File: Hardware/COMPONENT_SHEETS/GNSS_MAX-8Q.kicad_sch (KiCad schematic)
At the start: 12 parts, among them J2 Conn_Coaxial, Q1 SI1040X-T1-GE3, U4 MAX-8Q

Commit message: Corrected PCB edge cuts, removed components
Will be mimicking layout done by Seth Sievers
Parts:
- renumbered C4 to C5, C5 to C6, R3 to R1, R4 to R2, R5 to R3, U4 to U3
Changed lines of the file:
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@@
   (symbol (lib_id "Data_Collection_KiCAD_Project-rescue:GND-power-Data_Collection_KiCAD_Project-rescue") (at 101.6 165.1 0)
     (in_bom yes) (on_board yes)
-    (property "Reference" "#PWR018" (id 0) (at 101.6 171.45 0)
+    (property "Reference" "#PWR023" (id 0) (at 101.6 171.45 0)
       (effects (font (size 1.27 1.27)) hide)
     )
@@
   (symbol (lib_id "Data_Collection_KiCAD_Project-rescue:R-Device-Data_Collection_KiCAD_Project-rescue") (at 119.38 140.97 180)
     (in_bom yes) (on_board yes)
-    (property "Reference" "R5" (id 0) (at 117.602 142.1384 0)
+    (property "Reference" "R3" (id 0) (at 117.602 142.1384 0)
       (effects (font (size 1.27 1.27)) (justify left))
     )
@@
   (symbol (lib_id "Data_Collection_KiCAD_Project-rescue:R-Device-Data_Collection_KiCAD_Project-rescue") (at 110.49 158.75 0)
     (in_bom yes) (on_board yes)
-    (property "Reference" "R4" (id 0) (at 112.268 157.5816 0)
+    (property "Reference" "R2" (id 0) (at 112.268 157.5816 0)
       (effects (font (size 1.27 1.27)) (justify left))
     )
@@
   (symbol (lib_id "Data_Collection_KiCAD_Project-rescue:GND-power-Data_Collection_KiCAD_Project-rescue") (at 124.46 146.05 0)
     (in_bom yes) (on_board yes)
-    (property "Reference" "#PWR019" (id 0) (at 124.46 152.4 0)
+    (property "Reference" "#PWR024" (id 0) (at 124.46 152.4 0)
       (effects (font (size 1.27 1.27)) hide)
     )
@@
   (symbol (lib_id "Data_Collection_KiCAD_Project-rescue:R-Device-Data_Collection_KiCAD_Project-rescue") (at 92.71 140.97 0) (mirror y)
     (in_bom yes) (on_board yes)
-    (property "Reference" "R3" (id 0) (at 90.932 139.8016 0)
+    (property "Reference" "R1" (id 0) (at 90.932 139.8016 0)
       (effects (font (size 1.27 1.27)) (justify left))
     )
@@
   (symbol (lib_id "Data_Collection_KiCAD_Project-rescue:+3.3V-power-Data_Collection_KiCAD_Project-rescue") (at 182.88 60.96 0)
     (in_bom yes) (on_board yes)
-    (property "Reference" "#PWR021" (id 0) (at 182.88 64.77 0)
+    (property "Reference" "#PWR026" (id 0) (at 182.88 64.77 0)
       (effects (font (size 1.27 1.27)) hide)
     )
@@
   (symbol (lib_id "Data_Collection_KiCAD_Project-rescue:GND-power-Data_Collection_KiCAD_Project-rescue") (at 195.58 99.06 0)
     (in_bom yes) (on_board yes)
-    (property "Reference" "#PWR022" (id 0) (at 195.58 105.41 0)
+    (property "Reference" "#PWR027" (id 0) (at 195.58 105.41 0)
       (effects (font (size 1.27 1.27)) hide)
     )
@@
   (symbol (lib_id "Data_Collection_KiCAD_Project-rescue:MAX-8Q-RF_GPS-Data_Collection_KiCAD_Project-rescue") (at 195.58 81.28 0)
     (in_bom yes) (on_board yes)
-    (property "Reference" "U4" (id 0) (at 195.58 53.34 0))
+    (property "Reference" "U3" (id 0) (at 195.58 53.34 0))
     (property "Value" "MAX-8Q" (id 1) (at 195.58 55.88 0))
     (property "Footprint" "RF_GPS:ublox_MAX" (id 2) (at 205.74 97.79 0)
@@
   (symbol (lib_id "Data_Collection_KiCAD_Project-rescue:GND-power-Data_Collection_KiCAD_Project-rescue") (at 30.48 49.53 0)
     (in_bom yes) (on_board yes)
-    (property "Reference" "#PWR017" (id 0) (at 30.48 55.88 0)
+    (property "Reference" "#PWR022" (id 0) (at 30.48 55.88 0)
       (effects (font (size 1.27 1.27)) hide)
     )
@@
   (symbol (lib_id "Data_Collection_KiCAD_Project-rescue:C-Device-Data_Collection_KiCAD_Project-rescue") (at 30.48 43.18 0)
     (in_bom yes) (on_board yes)
-    (property "Reference" "C4" (id 0) (at 33.401 42.0116 0)
+    (property "Reference" "C5" (id 0) (at 33.401 42.0116 0)
       (effects (font (size 1.27 1.27)) (justify left))
     )
@@
   (symbol (lib_id "Data_Collection_KiCAD_Project-rescue:+3.3V-power-Data_Collection_KiCAD_Project-rescue") (at 30.48 36.83 0)
     (in_bom yes) (on_board yes)
-    (property "Reference" "#PWR016" (id 0) (at 30.48 40.64 0)
+    (property "Reference" "#PWR021" (id 0) (at 30.48 40.64 0)
       (effects (font (size 1.27 1.27)) hide)
     )
@@
   (symbol (lib_id "Data_Collection_KiCAD_Project-rescue:C-Device-Data_Collection_KiCAD_Project-rescue") (at 40.64 43.18 0)
     (in_bom yes) (on_board yes)
-    (property "Reference" "C5" (id 0) (at 43.561 42.0116 0)
+    (property "Reference" "C6" (id 0) (at 43.561 42.0116 0)
       (effects (font (size 1.27 1.27)) (justify left))
     )
@@
   (symbol (lib_id "Data_Collection_KiCAD_Project-rescue:GND-power-Data_Collection_KiCAD_Project-rescue") (at 238.76 86.36 0)
     (in_bom yes) (on_board yes)
-    (property "Reference" "#PWR023" (id 0) (at 238.76 92.71 0)
+    (property "Reference" "#PWR028" (id 0) (at 238.76 92.71 0)
       (effects (font (size 1.27 1.27)) hide)
     )
@@
   (symbol (lib_id "Data_Collection_KiCAD_Project-rescue:GND-power-Data_Collection_KiCAD_Project-rescue") (at 166.37 93.98 0)
     (in_bom yes) (on_board yes)
-    (property "Reference" "#PWR020" (id 0) (at 166.37 100.33 0)
-      (effects (font (size 1.27 1.27)) hide)
-    )
+    (property "Reference" "#PWR025" (id 0) (at 166.37 100.33 0)
+      (effects (font (size 1.27 1.27)) hide)
+    )

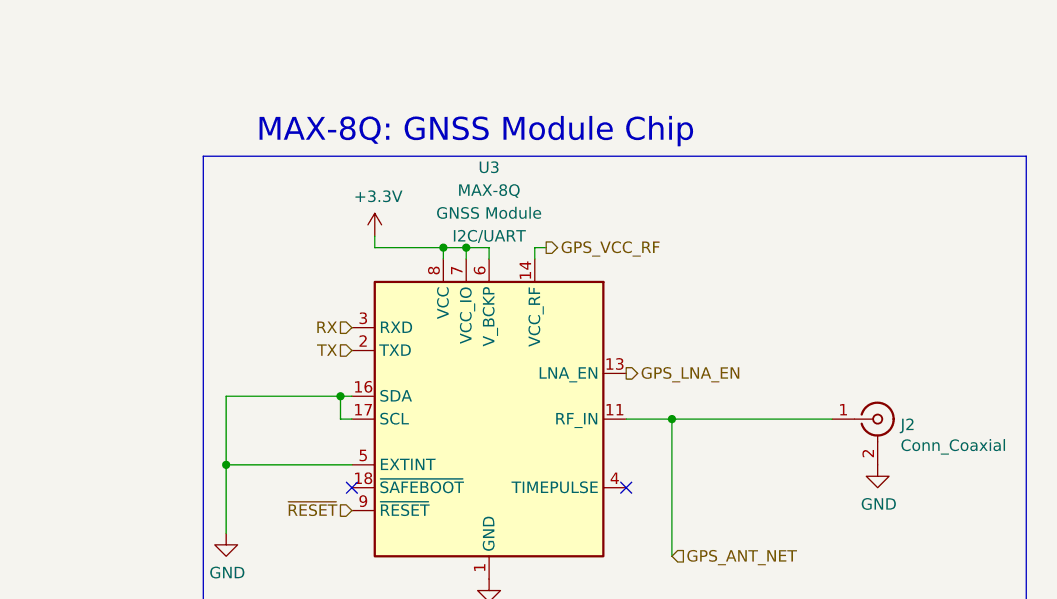
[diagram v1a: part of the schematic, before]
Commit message: Organized components, arranged filter caps
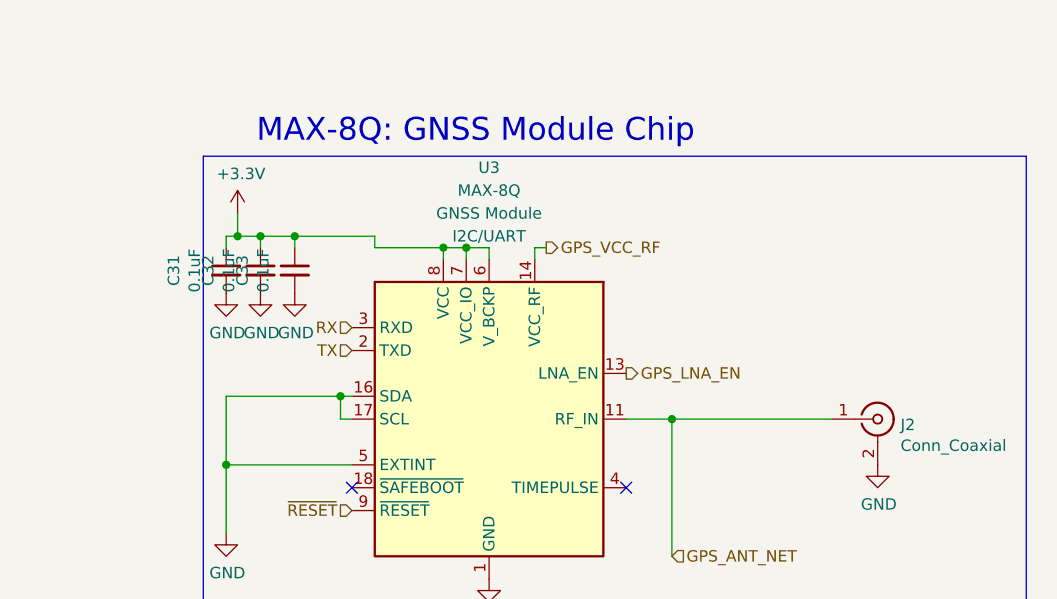
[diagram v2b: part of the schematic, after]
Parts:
- added C31, C32, C33: 0.1uF, Capacitor_SMD:C_0603_1608Metric_Pad1.08x0.95mm_HandSolder, symbol Data_Collection_KiCAD_Project-rescue:C_Small-Device-Data_Collection_KiCAD_Proje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
- Q1: footprint SC-89:SC-89 -> Package_TO_SOT_SMD:TSOT-23-6_HandSoldering
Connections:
- net +3V3: now also C31.1, C32.1, C33.1
- net GND: now also C31.2, C32.2, C33.2

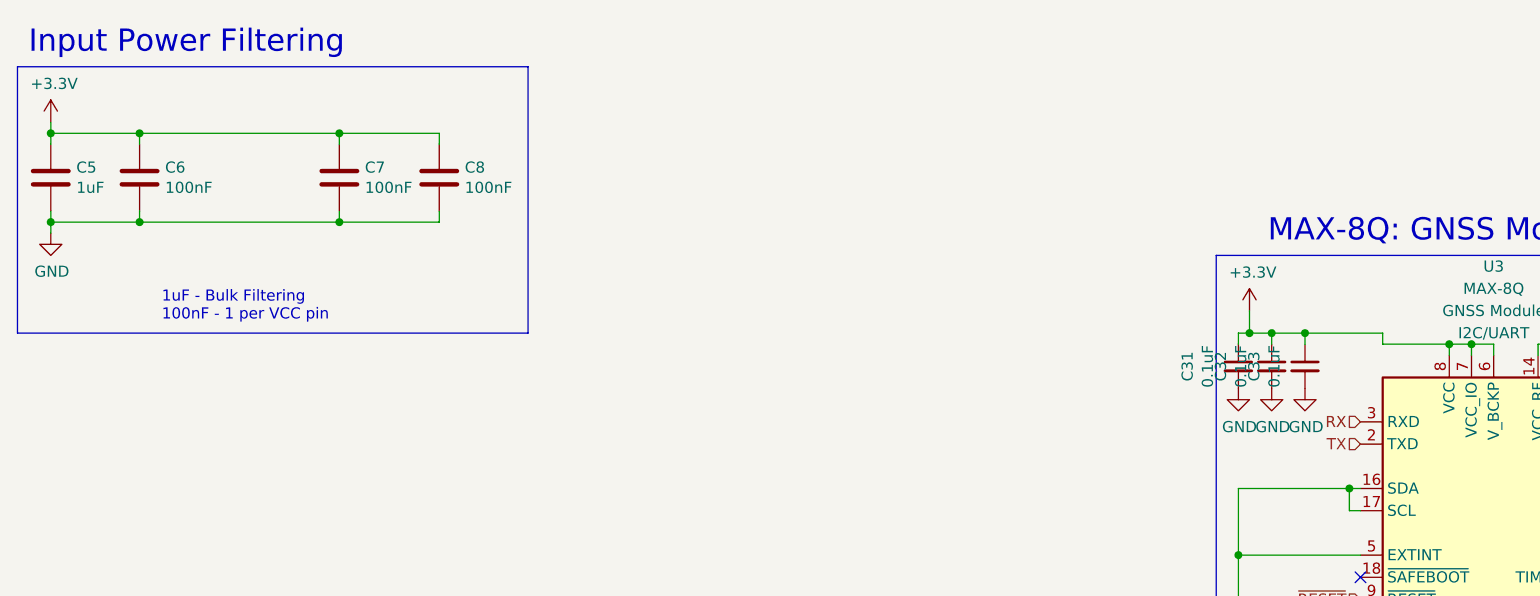
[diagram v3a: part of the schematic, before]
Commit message: Replaced Temp Sense and finalized routing
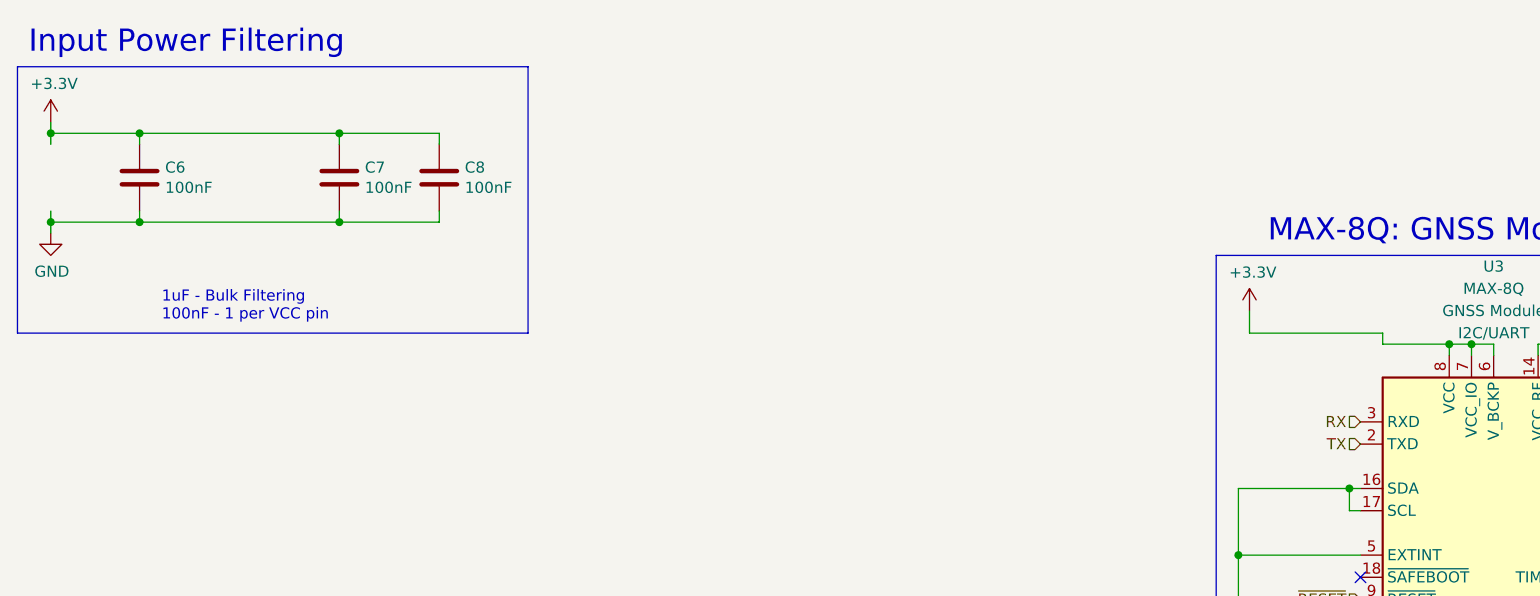
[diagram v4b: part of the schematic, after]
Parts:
- removed C31, C32, C33: 0.1uF, Capacitor_SMD:C_0603_1608Metric_Pad1.08x0.95mm_HandSolder, symbol Data_Collection_KiCAD_Project-rescue:C_Small-Device-Data_Collection_KiCAD_Proje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
- removed C5: 1uF, Capacitor_SMD:C_0603_1608Metric_Pad1.08x0.95mm_HandSolder, symbol Data_Collection_KiCAD_Project-rescue:C-Device-Data_Collection_KiCAD_Project-res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
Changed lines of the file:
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@@
     (comment 3 "Schematic depicting logical connections between components")
   )
-  (junction (at 170.18 60.96) (diameter 0) (color 0 0 0 0)
-  )
-  (junction (at 167.64 60.96) (diameter 0) (color 0 0 0 0)
-  )
   (junction (at 40.64 48.26) (diameter 0) (color 0 0 0 0)
   )
@@
   )
   (junction (at 166.37 86.36) (diameter 0) (color 0 0 0 0)
-  )
-  (junction (at 173.99 60.96) (diameter 0) (color 0 0 0 0)
   )
   (junction (at 101.6 163.83) (diameter 0) (color 0 0 0 0)
@@
     (stroke (width 0) (type default) (color 0 0 0 0))
   )
-  (wire (pts (xy 170.18 60.96) (xy 170.18 62.23))
-    (stroke (width 0) (type default) (color 0 0 0 0))
-  )
   (wire (pts (xy 182.88 62.23) (xy 190.5 62.23))
     (stroke (width 0) (type default) (color 0 0 0 0))
@@
     (stroke (width 0) (type default) (color 0 0 0 0))
   )
-  (wire (pts (xy 166.37 62.23) (xy 166.37 60.96))
-    (stroke (width 0) (type default) (color 0 0 0 0))
-  )
   (polyline (pts (xy 85.09 60.96) (xy 85.09 30.48))
     (stroke (width 0) (type default) (color 0 0 0 0))
@@
     (stroke (width 0) (type default) (color 0 0 0 0))
   )
-  (wire (pts (xy 182.88 60.96) (xy 173.99 60.96))
-    (stroke (width 0) (type default) (color 0 0 0 0))
-  )
-  (wire (pts (xy 173.99 60.96) (xy 173.99 62.23))
+  (wire (pts (xy 167.64 60.96) (xy 182.88 60.96))
     (stroke (width 0) (type default) (color 0 0 0 0))
   )
@@
     (stroke (width 0) (type default) (color 0 0 0 0))
   )
-  (wire (pts (xy 173.99 60.96) (xy 170.18 60.96))
-    (stroke (width 0) (type default) (color 0 0 0 0))
-  )
   (wire (pts (xy 30.48 48.26) (xy 30.48 49.53))
     (stroke (width 0) (type default) (color 0 0 0 0))
@@
     (stroke (width 0) (type default) (color 0 0 0 0))
   )
-  (wire (pts (xy 166.37 60.96) (xy 167.64 60.96))
-    (stroke (width 0) (type default) (color 0 0 0 0))
-  )
   (wire (pts (xy 179.07 81.28) (xy 179.07 78.74))
     (stroke (width 0) (type default) (color 0 0 0 0))
@@
   )
   (wire (pts (xy 193.04 62.23) (xy 195.58 62.23))
-    (stroke (width 0) (type default) (color 0 0 0 0))
-  )
-  (wire (pts (xy 170.18 60.96) (xy 167.64 60.96))
     (stroke (width 0) (type default) (color 0 0 0 0))
   )
@@
     (pin "1")
   )
-  (symbol (lib_id "Data_Collection_KiCAD_Project-rescue:C-Device-Data_Collection_KiCAD_Project-rescue") (at 30.48 43.18 0) (unit 1)
-    (in_bom yes) (on_board yes)
-    (property "Reference" "C5" (id 0) (at 33.401 42.0116 0)
-      (effects (font (size 1.27 1.27)) (justify left))
-    )
-    (property "Value" "1uF" (id 1) (at 33.401 44.323 0)
-      (effects (font (size 1.27 1.27)) (justify left))
-    )
-    (property "Footprint" "Capacitor_SMD:C_0603_1608Metric_Pad1.08x0.95mm_HandSolder" (id 2) (at 31.4452 46.99 0)
-      (effects (font (size 1.27 1.27)) hide)
-    )
-    (property "Datasheet" "~" (id 3) (at 30.48 43.18 0)
-      (effects (font (size 1.27 1.27)) hide)
-    )
-    (pin "1")
-    (pin "2")
-  )
   (symbol (lib_id "Data_Collection_KiCAD_Project-rescue:+3.3V-power-Data_Collection_KiCAD_Project-rescue") (at 30.48 36.83 0) (unit 1)
     (in_bom yes) (on_board yes)
@@
     (pin "1")
   )
-  (symbol (lib_id "Data_Collection_KiCAD_Project-rescue:GND-power-Data_Collection_KiCAD_Project-rescue") (at 170.18 67.31 0) (unit 1)
-    (in_bom yes) (on_board yes)
-    (property "Reference" "#PWR067" (id 0) (at 170.18 73.66 0)
-      (effects (font (size 1.27 1.27)) hide)
-    )
-    (property "Value" "GND" (id 1) (at 170.307 71.7042 0))
-    (property "Footprint" "" (id 2) (at 170.18 67.31 0)
-      (effects (font (size 1.27 1.27)) hide)
-    )
-    (property "Datasheet" "" (id 3) (at 170.18 67.31 0)
-      (effects (font (size 1.27 1.27)) hide)
-    )
-    (pin "1")
-  )
-  (symbol (lib_id "Data_Collection_KiCAD_Project-rescue:GND-power-Data_Collection_KiCAD_Project-rescue") (at 166.37 67.31 0) (unit 1)
-    (in_bom yes) (on_board yes)
-    (property "Reference" "#PWR066" (id 0) (at 166.37 73.66 0)
-      (effects (font (size 1.27 1.27)) hide)
-    )
-    (property "Value" "GND" (id 1) (at 166.497 71.7042 0))
-    (property "Footprint" "" (id 2) (at 166.37 67.31 0)
-      (effects (font (size 1.27 1.27)) hide)
-    )
-    (property "Datasheet" "" (id 3) (at 166.37 67.31 0)
-      (effects (font (size 1.27 1.27)) hide)
-    )
-    (pin "1")
-  )
-  (symbol (lib_id "Data_Collection_KiCAD_Project-rescue:C_Small-Device-Data_Collection_KiCAD_Project-rescue") (at 170.18 64.77 0) (unit 1)
-    (in_bom yes) (on_board yes)
-    (property "Reference" "C32" (id 0) (at 164.3634 64.77 90))
-    (property "Value" "0.1uF" (id 1) (at 166.6748 64.77 90))
-    (property "Footprint" "Capacitor_SMD:C_0603_1608Metric_Pad1.08x0.95mm_HandSolder" (id 2) (at 170.18 64.77 0)
-      (effects (font (size 1.27 1.27)) hide)
-    )
-    (property "Datasheet" "~" (id 3) (at 170.18 64.77 0)
-      (effects (font (size 1.27 1.27)) hide)
-    )
-    (pin "1")
-    (pin "2")
-  )
-  (symbol (lib_id "Data_Collection_KiCAD_Project-rescue:GND-power-Data_Collection_KiCAD_Project-rescue") (at 173.99 67.31 0) (unit 1)
-    (in_bom yes) (on_board yes)
-    (property "Reference" "#PWR068" (id 0) (at 173.99 73.66 0)
-      (effects (font (size 1.27 1.27)) hide)
-    )
-    (property "Value" "GND" (id 1) (at 174.117 71.7042 0))
-    (property "Footprint" "" (id 2) (at 173.99 67.31 0)
-      (effects (font (size 1.27 1.27)) hide)
-    )
-    (property "Datasheet" "" (id 3) (at 173.99 67.31 0)
-      (effects (font (size 1.27 1.27)) hide)
-    )
-    (pin "1")
-  )
-  (symbol (lib_id "Data_Collection_KiCAD_Project-rescue:C_Small-Device-Data_Collection_KiCAD_Project-rescue") (at 166.37 64.77 0) (unit 1)
-    (in_bom yes) (on_board yes)
-    (property "Reference" "C31" (id 0) (at 160.5534 64.77 90))
-    (property "Value" "0.1uF" (id 1) (at 162.8648 64.77 90))
-    (property "Footprint" "Capacitor_SMD:C_0603_1608Metric_Pad1.08x0.95mm_HandSolder" (id 2) (at 166.37 64.77 0)
-      (effects (font (size 1.27 1.27)) hide)
-    )
-    (property "Datasheet" "~" (id 3) (at 166.37 64.77 0)
-      (effects (font (size 1.27 1.27)) hide)
-    )
-    (pin "1")
-    (pin "2")
-  )
-  (symbol (lib_id "Data_Collection_KiCAD_Project-rescue:C_Small-Device-Data_Collection_KiCAD_Project-rescue") (at 173.99 64.77 0) (unit 1)
-    (in_bom yes) (on_board yes)
-    (property "Reference" "C33" (id 0) (at 168.1734 64.77 90))
-    (property "Value" "0.1uF" (id 1) (at 170.4848 64.77 90))
-    (property "Footprint" "Capacitor_SMD:C_0603_1608Metric_Pad1.08x0.95mm_HandSolder" (id 2) (at 173.99 64.77 0)
-      (effects (font (size 1.27 1.27)) hide)
-    )
-    (property "Datasheet" "~" (id 3) (at 173.99 64.77 0)
-      (effects (font (size 1.27 1.27)) hide)
-    )
-    (pin "1")
-    (pin "2")
-  )
 )

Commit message: Corrected Si1040X Footprint
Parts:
- Q1: footprint Package_TO_SOT_SMD:TSOT-23-6_HandSoldering -> Package_TO_SOT_SMD:SOT-563
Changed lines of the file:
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@@
     (property "Reference" "Q1" (id 0) (at 101.6 129.7432 0))
     (property "Value" "SI1040X-T1-GE3" (id 1) (at 101.6 132.0546 0))
-    (property "Footprint" "Package_TO_SOT_SMD:TSOT-23-6_HandSoldering" (id 2) (at 102.87 158.115 0)
+    (property "Footprint" "Package_TO_SOT_SMD:SOT-563" (id 2) (at 102.87 158.115 0)
       (effects (font (size 1.27 1.27)) hide)
     )
